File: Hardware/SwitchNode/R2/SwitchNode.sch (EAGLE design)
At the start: 18 parts, among them T1 2SC1815, T2 2SC1815, T3 C1815

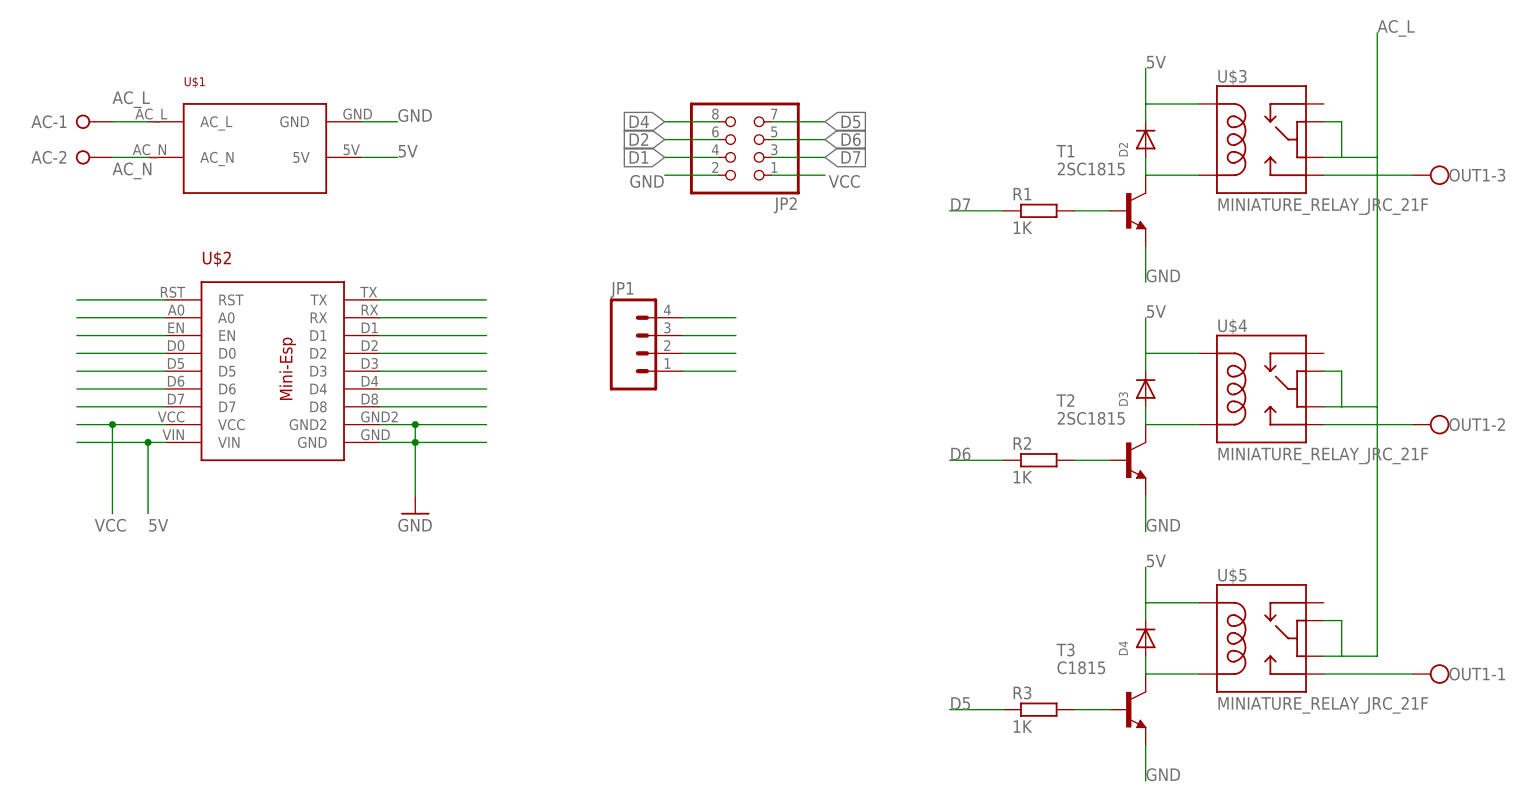
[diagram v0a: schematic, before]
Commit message: Correct PSU pinouts and update labels for SwitchNode R2
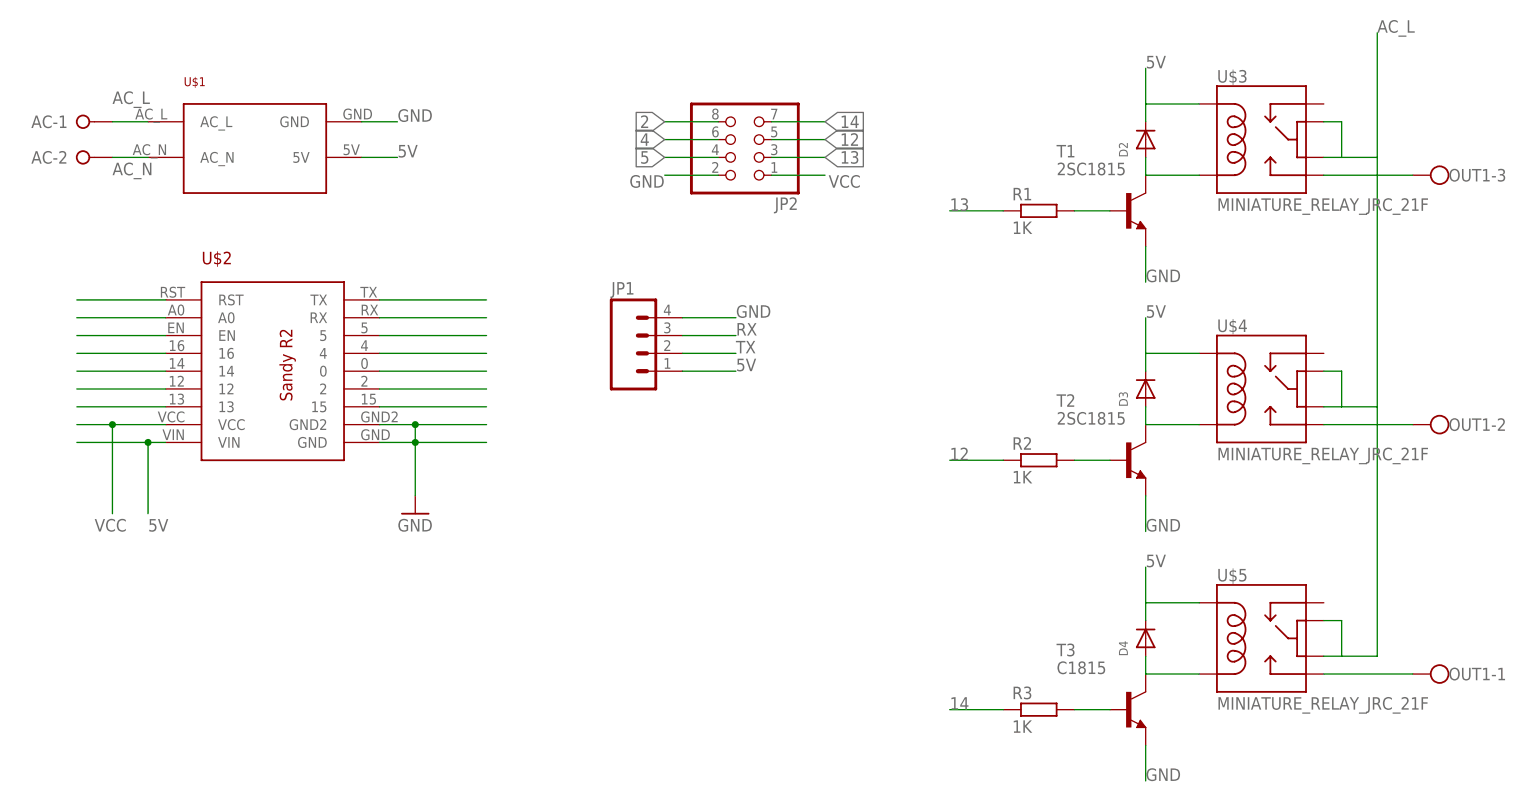
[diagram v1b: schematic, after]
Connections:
- removed net D0: U$2.D0
- removed net D1: JP2.4, U$2.D1
- removed net D2: JP2.6, U$2.D2
- removed net D3: U$2.D3
- removed net D4: JP2.8, U$2.D4
- removed net D5: JP2.7, R3.1, U$2.D5
- removed net D6: JP2.5, R2.1, U$2.D6
- removed net D7: JP2.3, R1.1, U$2.D7
- new net 0: U$2.0
- new net 12: JP2.5, R2.1, U$2.12
- new net 13: JP2.3, R1.1, U$2.13
- new net 14: JP2.7, R3.1, U$2.14
- new net 16: U$2.16
- new net 2: JP2.8, U$2.2
- new net 4: JP2.6, U$2.4
- new net 5: JP2.4, U$2.5
- net D8: now also U$2.15; no longer U$2.D8
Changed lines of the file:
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@@
 <pinref part="JP1" gate="G$1" pin="4"/>
 <wire x1="193.04" y1="119.38" x2="200.66" y2="119.38" width="0.1524" layer="91"/>
+<label x="200.66" y="119.38" size="1.778" layer="95"/>
 </segment>
 </net>
@@
 <pinref part="JP1" gate="G$1" pin="1"/>
 <wire x1="193.04" y1="111.76" x2="200.66" y2="111.76" width="0.1524" layer="91"/>
+<label x="200.66" y="111.76" size="1.778" layer="95"/>
 </segment>
 </net>
@@
 </segment>
 </net>
-<net name="D0" class="0">
+<net name="16" class="0">
 <segment>
-<pinref part="U$2" gate="G$1" pin="D0"/>
+<pinref part="U$2" gate="G$1" pin="16"/>
 <wire x1="119.38" y1="114.3" x2="106.68" y2="114.3" width="0.1524" layer="91"/>
 </segment>
@@
 <pinref part="JP1" gate="G$1" pin="2"/>
 <wire x1="193.04" y1="114.3" x2="200.66" y2="114.3" width="0.1524" layer="91"/>
+<label x="200.66" y="114.3" size="1.778" layer="95"/>
 </segment>
 </net>
@@
 <pinref part="JP1" gate="G$1" pin="3"/>
 <wire x1="193.04" y1="116.84" x2="200.66" y2="116.84" width="0.1524" layer="91"/>
+<label x="200.66" y="116.84" size="1.778" layer="95"/>
 </segment>
 </net>
-<net name="D2" class="0">
+<net name="4" class="0">
 <segment>
-<pinref part="U$2" gate="G$1" pin="D2"/>
+<pinref part="U$2" gate="G$1" pin="4"/>
 <wire x1="149.86" y1="114.3" x2="165.1" y2="114.3" width="0.1524" layer="91"/>
 </segment>
@@
 </segment>
 </net>
-<net name="D1" class="0">
+<net name="5" class="0">
 <segment>
-<pinref part="U$2" gate="G$1" pin="D1"/>
+<pinref part="U$2" gate="G$1" pin="5"/>
 <wire x1="149.86" y1="116.84" x2="165.1" y2="116.84" width="0.1524" layer="91"/>
 </segment>
@@
 </segment>
 </net>
-<net name="D3" class="0">
+<net name="0" class="0">
 <segment>
-<pinref part="U$2" gate="G$1" pin="D3"/>
+<pinref part="U$2" gate="G$1" pin="0"/>
 <wire x1="149.86" y1="111.76" x2="165.1" y2="111.76" width="0.1524" layer="91"/>
 </segment>
 </net>
-<net name="D4" class="0">
+<net name="2" class="0">
 <segment>
-<pinref part="U$2" gate="G$1" pin="D4"/>
+<pinref part="U$2" gate="G$1" pin="2"/>
 <wire x1="149.86" y1="109.22" x2="165.1" y2="109.22" width="0.1524" layer="91"/>
 </segment>
@@
 <net name="D8" class="0">
 <segment>
-<pinref part="U$2" gate="G$1" pin="D8"/>
+<pinref part="U$2" gate="G$1" pin="15"/>
 <wire x1="149.86" y1="106.68" x2="165.1" y2="106.68" width="0.1524" layer="91"/>
 </segment>
 </net>
-<net name="D7" class="0">
+<net name="13" class="0">
 <segment>
 <pinref part="R1" gate="G$1" pin="1"/>
@@
 </segment>
 <segment>
-<pinref part="U$2" gate="G$1" pin="D7"/>
+<pinref part="U$2" gate="G$1" pin="13"/>
 <wire x1="119.38" y1="106.68" x2="106.68" y2="106.68" width="0.1524" layer="91"/>
 </segment>
@@
 </segment>
 </net>
-<net name="D6" class="0">
+<net name="12" class="0">
 <segment>
-<pinref part="U$2" gate="G$1" pin="D6"/>
+<pinref part="U$2" gate="G$1" pin="12"/>
 <wire x1="119.38" y1="109.22" x2="106.68" y2="109.22" width="0.1524" layer="91"/>
 </segment>
@@
 </segment>
 </net>
-<net name="D5" class="0">
+<net name="14" class="0">
 <segment>
-<pinref part="U$2" gate="G$1" pin="D5"/>
+<pinref part="U$2" gate="G$1" pin="14"/>
 <wire x1="119.38" y1="111.76" x2="106.68" y2="111.76" width="0.1524" layer="91"/>
 </segment>
